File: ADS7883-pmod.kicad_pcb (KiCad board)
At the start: 2 copper layers, 34 x 28 mm, 78 parts, among them P1 CONN_01X03, P2 CONN_01X02, P3 CONN_01X02, P4 CONN_01X02, P5 CONN_02X06, U1 ref5050

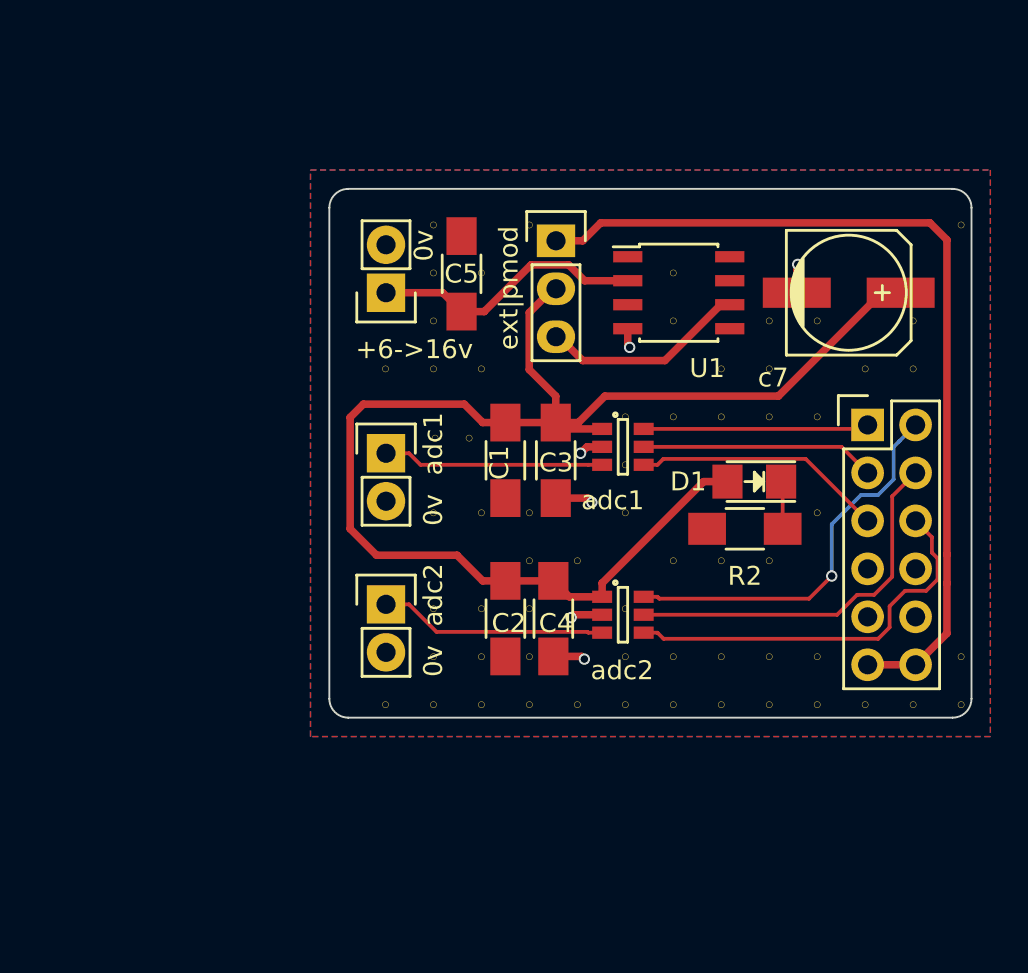
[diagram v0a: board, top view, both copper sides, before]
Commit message: convert to 4 layers and improve routing
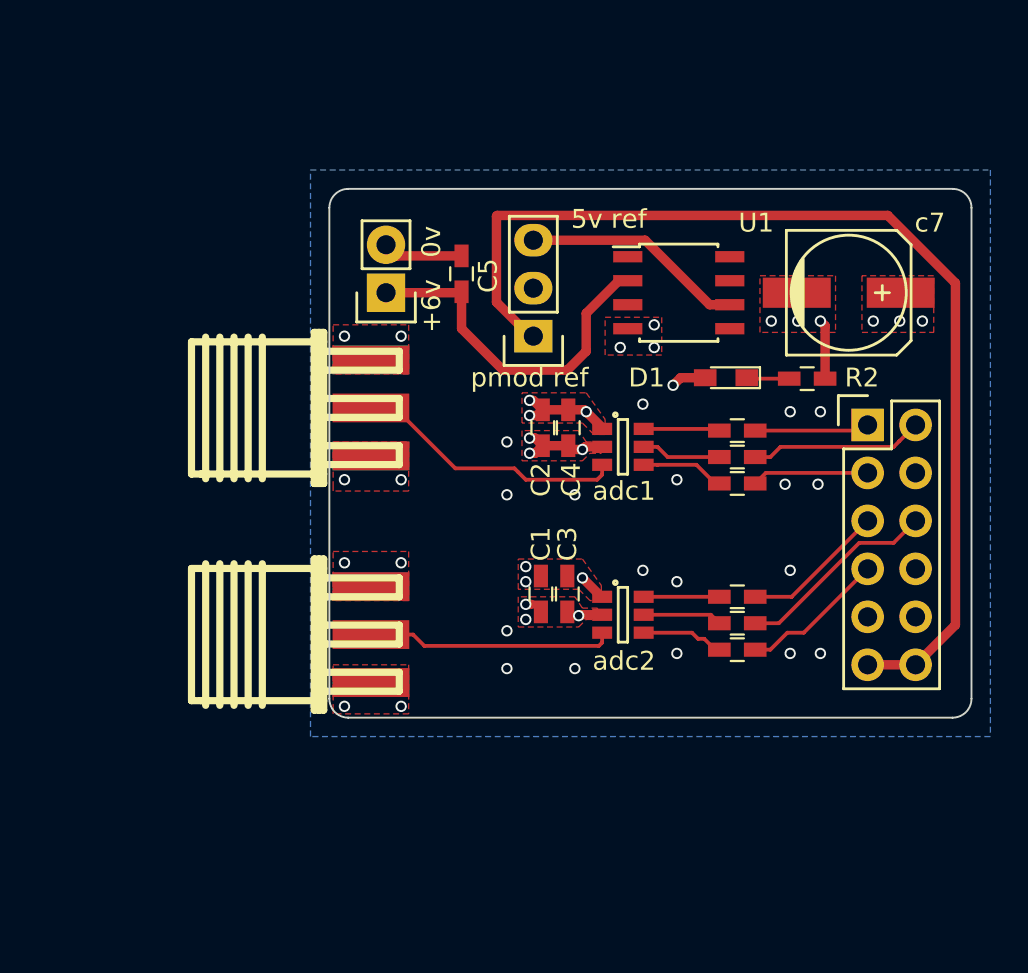
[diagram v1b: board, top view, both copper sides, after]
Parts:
- removed V10_10, V10_12, V10_13, V10_5, V10_6, V10_7, V11_12, V11_13, V11_5, V11_7, V11_9, V12_13, V12_6, V13_13, V13_5, V13_6, V14_12, V14_13, V14_3, V2_13, V2_6, V3_11, V3_12, V3_13, V3_3, V3_4, V3_5, V3_6, V3_9, V4_11, V4_12, V4_13, V4_4, V4_6, V4_9 (x3), V5_10, V5_11, V5_12, V5_13, V5_3, V5_9, V6_10, V6_13, V7_11, V7_12, V7_13, V7_7, V7_8, V7_9, V8_10, V8_12, V8_13, V8_4, V8_5, V8_7, V9_10, V9_12, V9_13, V9_6, V9_7: AUTO_VIA, VIA_MATRIX
- added R1: R, Capacitors_SMD:C_0603_HandSoldering, F.Cu at (149.6, 80.8)
- added R3: R, Capacitors_SMD:C_0603_HandSoldering, F.Cu at (149.6, 82.2)
- added R4: R, Capacitors_SMD:C_0603_HandSoldering, F.Cu at (149.6, 83.6)
- added R5: R, Capacitors_SMD:C_0603_HandSoldering, F.Cu at (149.6, 89.6)
- added R6: R, Capacitors_SMD:C_0603_HandSoldering, F.Cu at (149.6, 91.0)
- added R7: R, Capacitors_SMD:C_0603_HandSoldering, F.Cu at (149.6, 92.4)
- C1, C2, C3, C4, C5: footprint ADS7883:C_1206_HandSoldering -> Capacitors_SMD:C_0603_HandSoldering
- D1: footprint ADS7883:LED-1206 -> LEDs:LED_0603_HandSoldering
- P3, P4: footprint ADS7883:Pin_Header_Straight_1x02 -> ADS7883:CON-SMA-EDGE
- R2: footprint ADS7883:R_1206_HandSoldering -> Capacitors_SMD:C_0603_HandSoldering
- moved C2 10.3 mm to (139.3, 80.7)
- moved C4 10.1 mm to (140.7, 80.7)
- moved R2 8.61 mm to (153.3, 78.0), turned to 0 degrees
- moved C1 7.32 mm to (139.2, 89.5)
- moved C3 7.10 mm to (140.6, 89.5)
- moved D1 5.70 mm to (149.0, 78.0)
- moved P1 5.19 mm to (138.8, 75.8), turned to 180 degrees
- moved P3 2.53 mm to (130.2, 79.6), turned to 270 degrees
- moved P4 1.79 mm to (130.2, 91.6), turned to 270 degrees
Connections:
- P5 pad 1: adc1-cs -> Net-(P5-Pad1)
- P5 pad 2: adc2-cs -> Net-(P5-Pad2)
- P5 pad 3: adc1-sdo -> Net-(P5-Pad3)
- P5 pad 4: adc2-sdo -> Net-(P5-Pad4)
- P5 pad 5: adc1-clk -> Net-(P5-Pad5)
- P5 pad 6: adc2-clk -> Net-(P5-Pad6)
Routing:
- net adc-5v: track 74.0 -> 9.66 mm, vias 0 -> 10
- net adc2-cs: track 20.9 -> 4.01 mm, vias 1 -> 0
- net adc2-clk: track 21.2 -> 4.38 mm
- net adc2-sdo: track 20.0 -> 4.19 mm
- net Net-(P5-Pad6): track 0.00 -> 10.7 mm
- net pmod+: track 47.2 -> 56.7 mm
- net Net-(P5-Pad2): track 0.00 -> 9.19 mm
- net adc1-clk: track 13.3 -> 4.42 mm
- net adc1-sdo: track 12.4 -> 4.23 mm
- net adc1-cs: track 11.9 -> 4.04 mm
- net Net-(P5-Pad7): track 0.00 -> 7.72 mm
- net Net-(P5-Pad5): track 0.00 -> 7.62 mm
- net Net-(P5-Pad3): track 0.00 -> 6.87 mm
- net Net-(P5-Pad1): track 0.00 -> 6.37 mm
- net Earth: track 9.24 -> 14.0 mm, vias 6 -> 38
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- added copper zone on In1.Cu, net Earth
- added copper zone on F.Cu, net adc-5v
- added copper zone on In2.Cu, net adc-5v
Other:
- copper layers 2 -> 4
- net class power: trace_width 0.4 -> 0.5
- board text added: "+6v"
- board text added: "0v 0v +v +v"
- board text added: "5v ref"
- board text added: "ADS7883 PMOD breakout 4/2019 @matthewvenn"
- board text added: "a1sd a1cs a1ck"
- board text added: "a2sd a2cs a2ck"
- board text added: "pmod ref"
- board text removed: "+6->16v"
- board text removed: "ADS7883 PMOD breakout 7/2018 @matthewvenn"
- board text removed: "a2cs a1cs a2do a1do a2ck a1ck 0v 0v +v +v"
- board text removed: "adc1"
- board text removed: "adc2"
- board text removed: "ext|pmod"

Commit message: got rid of 1 ADC and added phantom and shield can
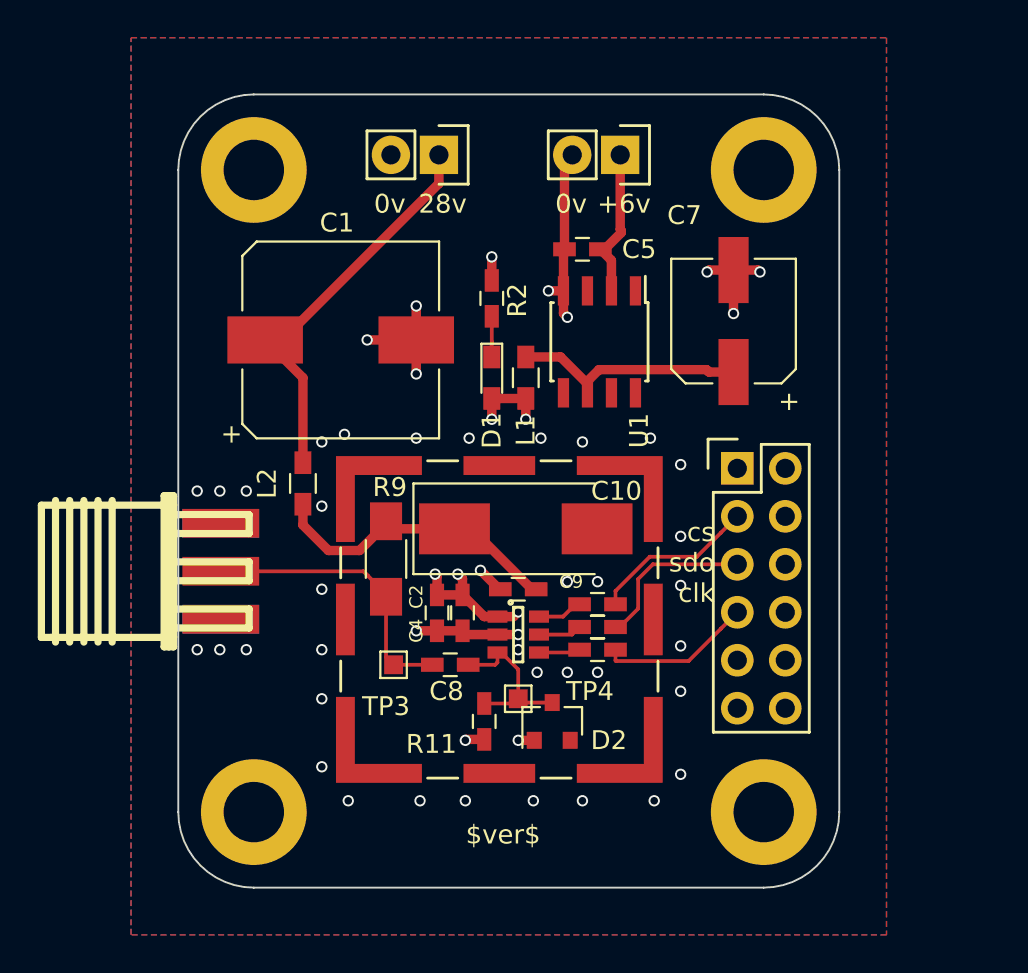
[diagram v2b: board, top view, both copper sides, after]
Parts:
- removed C3: 10n, Capacitors_SMD:C_0603_HandSoldering
- removed P1: CONN_01X03, ADS7883:Pin_Header_Straight_1x03
- removed P3: CONN_01X02, ADS7883:CON-SMA-EDGE
- removed R1, R3, R4: R, Capacitors_SMD:C_0603_HandSoldering
- removed adc2: ads7883, ADS7883:SOT-23-6
- removed c7: 22u, ADS7883:c_elec_6.3x7.7
- added C10: 22u, 35v, Capacitors_Tantalum_SMD:CP_Tantalum_Case-D_EIA-7343-31_Hand, F.Cu at (138.4, 86.0)
- added C7: 470uF 6.3v, Capacitors_SMD:CP_Elec_6.3x7.7, F.Cu at (149.4, 75.0)
- added C8: 0.1u, Capacitors_SMD:C_0603_HandSoldering, F.Cu at (134.4, 93.2)
- added C9: 0.1u, 100v, Capacitors_SMD:C_0603_HandSoldering, F.Cu at (138.0, 89.2)
- added D2: 260mv schottky, Diodes_SMD:D_SOT-23_ANK, F.Cu at (139.8, 96.2)
- added J1: RF_Shield_Two_Pieces, Shielding_Cabinets:Laird_Technologies_BMI-S-102_16.50x16.50mm, F.Cu at (137.0, 90.8)
- added J2: Conn_01x01, Mounting_Holes:MountingHole_3.2mm_M3_DIN965_Pad, F.Cu at (151.0, 67.0)
- added J3: Conn_01x01, Mounting_Holes:MountingHole_3.2mm_M3_DIN965_Pad, F.Cu at (151.0, 101.0)
- added J4: Conn_01x01, Mounting_Holes:MountingHole_3.2mm_M3_DIN965_Pad, F.Cu at (124.0, 101.0)
- added J5: Conn_01x01, Mounting_Holes:MountingHole_3.2mm_M3_DIN965_Pad, F.Cu at (124.0, 67.0)
- added L1: L_Small, Inductors_SMD:L_0603_HandSoldering, F.Cu at (138.4, 78.0)
- added L2: L_Small, Inductors_SMD:L_0603_HandSoldering, F.Cu at (126.6, 83.6)
- added P6: CONN_01X02, ADS7883:Pin_Header_Straight_1x02, F.Cu at (143.4, 66.2)
- added R11: 10k, Capacitors_SMD:C_0603_HandSoldering, F.Cu at (136.2, 96.2)
- added R9: 50R, Resistors_SMD:R_1206_HandSoldering, F.Cu at (131.0, 87.6)
- added TP3: TEST, Connectors_TestPoints:Test_Point_Pad_1.0x1.0mm, F.Cu at (131.4, 93.2)
- added TP4: TEST, Connectors_TestPoints:Test_Point_Pad_1.0x1.0mm, F.Cu at (138.0, 95.0)
- C1: value 1u -> 470uF 35v; footprint Capacitors_SMD:C_0603_HandSoldering -> Capacitors_SMD:CP_Elec_10x10
- moved R2 17.2 mm to (136.6, 73.8), turned to 90 degrees
- moved C1 17.1 mm to (128.6, 76.0), turned to 0 degrees
- moved D1 12.4 mm to (136.6, 78.0), turned to 270 degrees
- moved adc1 11.4 mm to (138.0, 91.6)
- moved C2 11.3 mm to (133.7, 90.5)
- moved C4 11.3 mm to (135.1, 90.5)
- moved P4 8.63 mm to (122.2, 88.2)
- moved P2 7.82 mm to (133.8, 66.2), turned to 270 degrees
- moved R5 7.41 mm to (142.2, 90.0)
- moved R6 7.40 mm to (142.2, 91.2)
- moved R7 7.40 mm to (142.2, 92.4)
- moved P5 7.27 mm to (149.6, 82.8)
- moved C5 6.53 mm to (141.4, 71.2), turned to 180 degrees
- moved U1 4.94 mm to (142.3, 76.1), turned to 270 degrees
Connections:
- C1 pad 1: adc-5v -> Net-(C1-Pad1)
- P2 pad 1: +12V -> Net-(C1-Pad1)
- P5 pad 11: pmod+ -> Net-(P5-Pad11)
- P5 pad 12: pmod+ -> Net-(P5-Pad12)
- R5 pad 1: Net-(P5-Pad5) -> Net-(P5-Pad3)
- R6 pad 2: Net-(P5-Pad6) -> Net-(P5-Pad5)
- U1 pad 6: ref-5v -> Net-(C7-Pad1)
- adc1 pad 4: adc1-clk -> adc2-clk
- adc1 pad 5: adc1-sdo -> adc2-sdo
- adc1 pad 6: adc1-cs -> adc2-cs
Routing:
- net pmod+: track 56.7 -> 0.00 mm
- net Earth: track 14.0 -> 40.2 mm, vias 38 -> 50
- net Net-(C1-Pad1): track 0.00 -> 21.5 mm
- net phantom: track 0.00 -> 18.0 mm
- net Net-(C7-Pad1): track 0.00 -> 13.0 mm
- net ref-5v: track 11.8 -> 0.00 mm
- net +12V: track 18.8 -> 8.05 mm
- net Net-(P5-Pad6): track 10.7 -> 0.00 mm
- net Net-(P5-Pad2): track 9.19 -> 0.00 mm
- net Net-(P5-Pad1): track 6.37 -> 0.00 mm
- net Net-(C8-Pad2): track 14.5 -> 9.15 mm
- net adc1-clk: track 4.42 -> 0.00 mm
- net adc1-sdo: track 4.23 -> 0.00 mm
- net adc1-cs: track 4.04 -> 0.00 mm
- net Net-(C8-Pad1): track 13.1 -> 15.4 mm
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- removed copper zone on F.Cu, net adc-5v
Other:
- board size 34 x 28 mm -> 35 x 42 mm
- board text added: "28v"
- board text added: "cs sdo clk"
- board text removed: "5v ref"
- board text removed: "a1sd a1cs a1ck"
- board text removed: "a2sd a2cs a2ck"
- board text removed: "pmod ref"
